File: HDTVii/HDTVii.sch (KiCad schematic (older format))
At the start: 30 parts

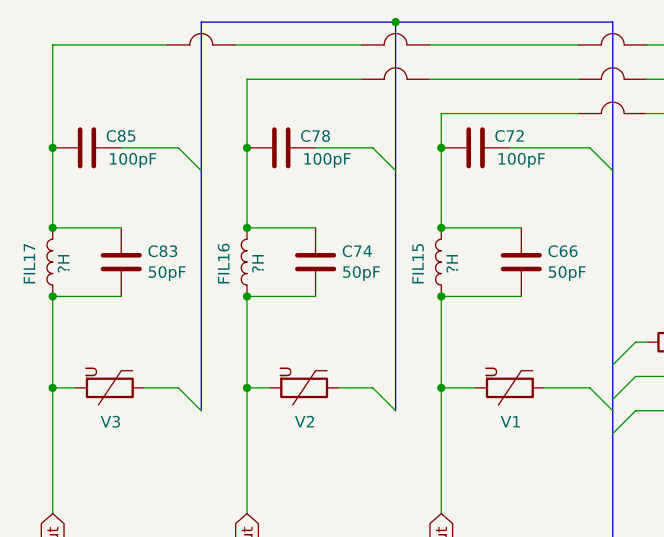
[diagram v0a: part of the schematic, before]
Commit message: Added correct (hopefully) inductor values. Credit to Job Feikens for the values
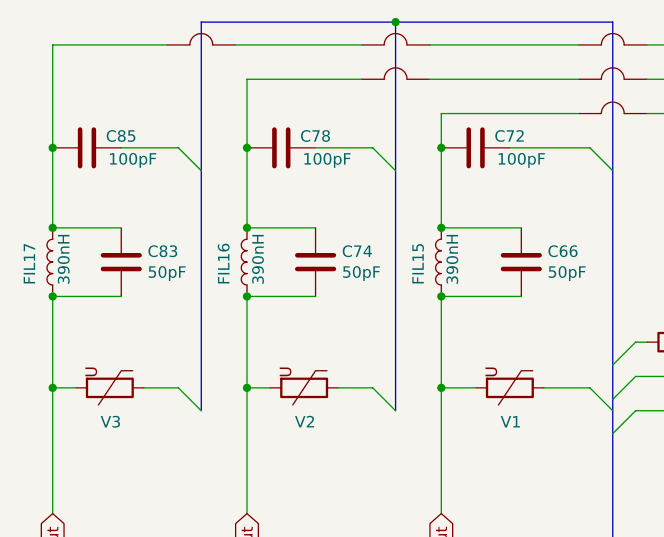
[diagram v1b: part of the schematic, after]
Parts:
- FIL15, FIL16, FIL17: value ?H -> 390nH
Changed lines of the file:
@@
 EESchema Schematic File Version 4
-LIBS:HDTVii-cache
-EELAYER 26 0
+EELAYER 30 0
 EELAYER END
 $Descr A4 11693 8268
@@
 	5350 4350 5350 4900
 Wire Wire Line
-	3650 3950 3650 4350
-Wire Wire Line
 	3650 4350 3750 4350
-Connection ~ 3650 4350
 Wire Wire Line
 	3650 4350 3650 4900
@@
 P 3650 3800
 F 0 "FIL17" V 3750 3900 50  0000 R CNN
-F 1 "?H" V 3600 3850 50  0000 R CNN
+F 1 "390nH" V 3600 3900 50  0000 R CNN
 F 2 "Inductor_SMD:L_0603_1608Metric_Pad1.05x0.95mm_HandSolder" H 3650 3800 50  0001 C CNN
 F 3 "~" H 3650 3800 50  0001 C CNN
@@
 	-1   0    0    1
 $EndComp
-Connection ~ 3650 3950
 $Comp
 L Device:L FIL16
@@
 P 4500 3800
 F 0 "FIL16" V 4600 3900 50  0000 R CNN
-F 1 "?H" V 4450 3850 50  0000 R CNN
+F 1 "390nH" V 4450 3900 50  0000 R CNN
 F 2 "Inductor_SMD:L_0603_1608Metric_Pad1.05x0.95mm_HandSolder" H 4500 3800 50  0001 C CNN
 F 3 "~" H 4500 3800 50  0001 C CNN
@@
 P 5350 3800
 F 0 "FIL15" V 5450 3900 50  0000 R CNN
-F 1 "?H" V 5300 3850 50  0000 R CNN
+F 1 "390nH" V 5300 3900 50  0000 R CNN
 F 2 "Inductor_SMD:L_0603_1608Metric_Pad1.05x0.95mm_HandSolder" H 5350 3800 50  0001 C CNN
 F 3 "~" H 5350 3800 50  0001 C CNN
@@
 Text GLabel 7950 4900 3    50   Input ~ 0
 AVE54
+Wire Wire Line
+	3650 3950 3650 4350
 Wire Bus Line
 	4300 2750 4300 4450
@@
 Wire Bus Line
 	6100 2750 6100 5250
+Connection ~ 3650 3950
+Connection ~ 3650 4350
 $EndSCHEMATC

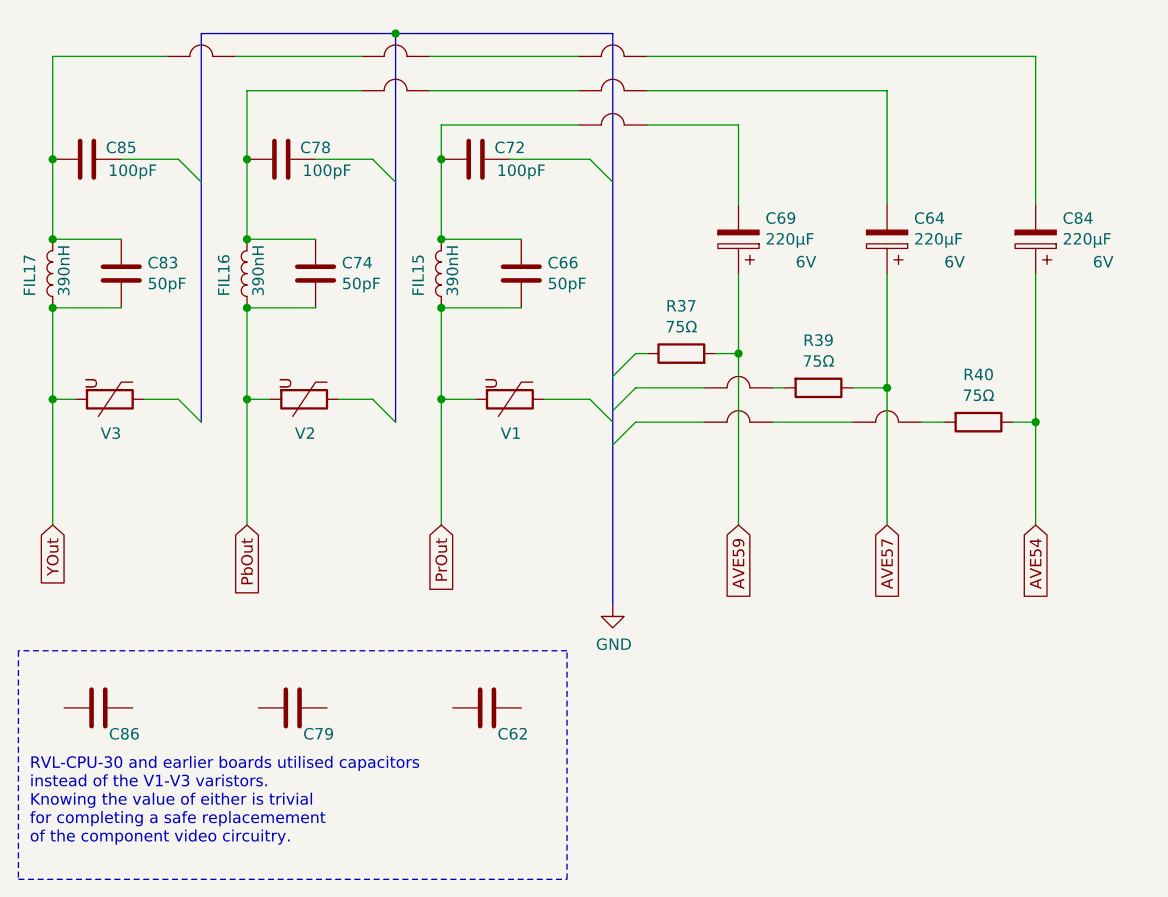
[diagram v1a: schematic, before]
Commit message: Created PCB design and added footprint refs to parts.
Also changed stuff in the Schematic
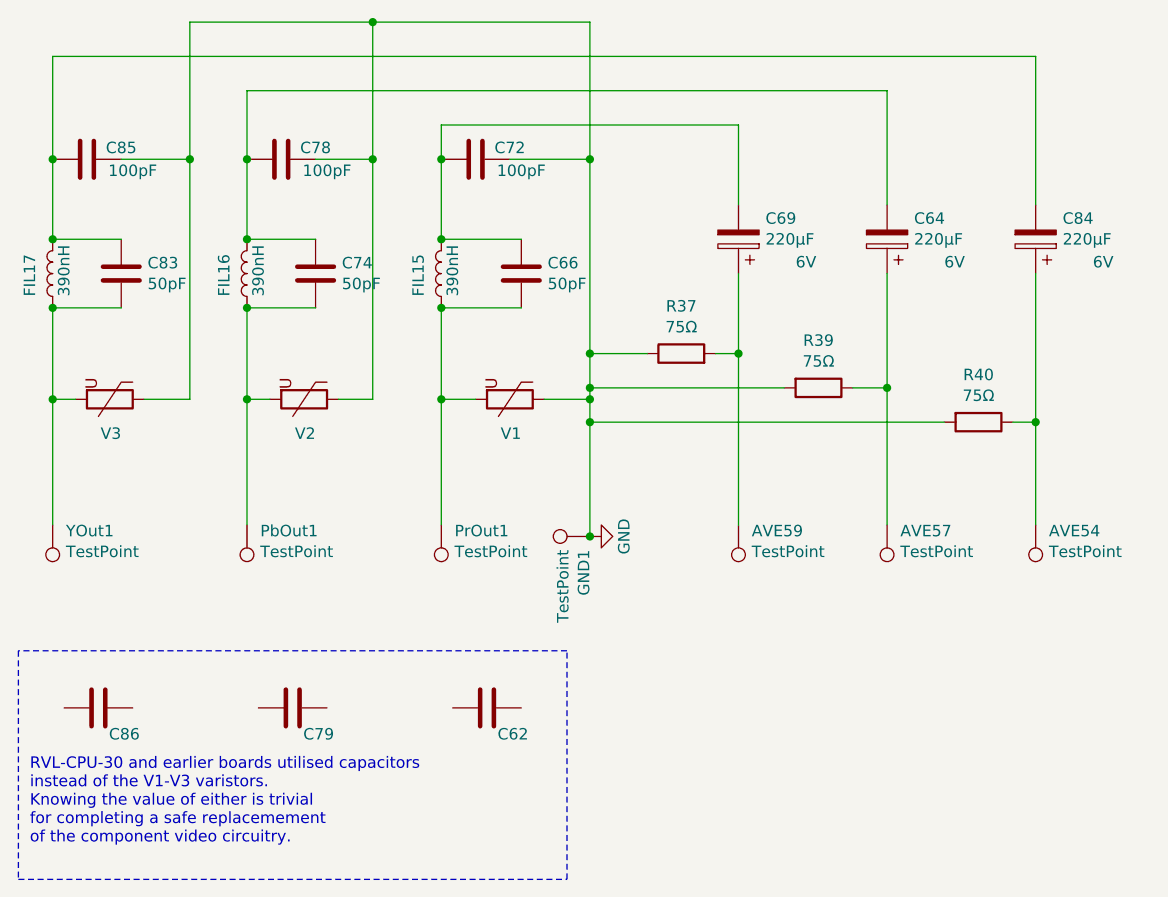
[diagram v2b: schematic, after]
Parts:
- removed W1, W2, W3, W4, W5, W6, W7, W8, W9: Wire_Arc, symbol HDTVii-rescue:Wire_Arc-My_Library
- added AVE54, AVE57, AVE59, GND1, PbOut1, PrOut1, YOut1: TestPoint, Connector_Pin:Pin_D1.0mm_L10.0mm, symbol Connector:TestPoint
- C64, C69, C84: footprint Capacitor_SMD:CP_Elec_6.3x3 -> Capacitor_SMD:CP_Elec_8x10.5
- FIL15, FIL16, FIL17: footprint Inductor_SMD:L_0603_1608Metric_Pad1.05x0.95mm_HandSolder -> Inductor_SMD:L_0402_1005Metric
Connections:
- net GND: now also C72.1, C78.1, C85.1, R37.1, R39.2, R40.2, V1.1, V2.1, V3.1, GND1.1
- net at C66.1, C72.2, FIL15.2: now also C69.2
- net at C74.1, C78.2, FIL16.2: now also C64.2
- net at C83.1, C85.2, FIL17.2: now also C84.2
- net AVE54: no longer names the net of C84.1, R40.1
- net AVE54: now also AVE54.1
- net AVE57: no longer names the net of C64.1, R39.1
- net AVE57: now also AVE57.1
- net AVE59: no longer names the net of C69.1, R37.2
- net AVE59: now also AVE59.1
- net PbOut: no longer names the net of C74.2, FIL16.1, V2.2
- net PbOut: now also PbOut1.1
- net PrOut: no longer names the net of C66.2, FIL15.1, V1.2
- net PrOut: now also PrOut1.1
- net YOut: no longer names the net of C83.2, FIL17.1, V3.2
- net YOut: now also YOut1.1
